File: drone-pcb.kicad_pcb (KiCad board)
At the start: 2 copper layers, 46 parts, among them J1 Conn_01x02_Pin, J10 Conn_01x03_Pin, J11 Conn_01x03_Pin, J12 Conn_01x03_Pin, J2 Conn_01x02_Pin, J3 Conn_01x02_Pin, J4 Conn_01x02_Pin, J5 Conn_01x02_Pin, J6 Conn_01x02_Pin, J7 USB_C_Receptacle_USB2.0_16P, J8 Conn_01x02_Pin, J9 Conn_01x03_Pin, Q1 AO3400A, Q2 AO3400A, Q3 AO3400A, Q4 AO3400A, Q5 AO3400A, Q6 AO3400A, SW1 CK_KMS2xxGP, U1 STM32F030C8Tx, U2 nRF24L01P, U3 MCP73831-2-OT, U4 TLV75533PDBV

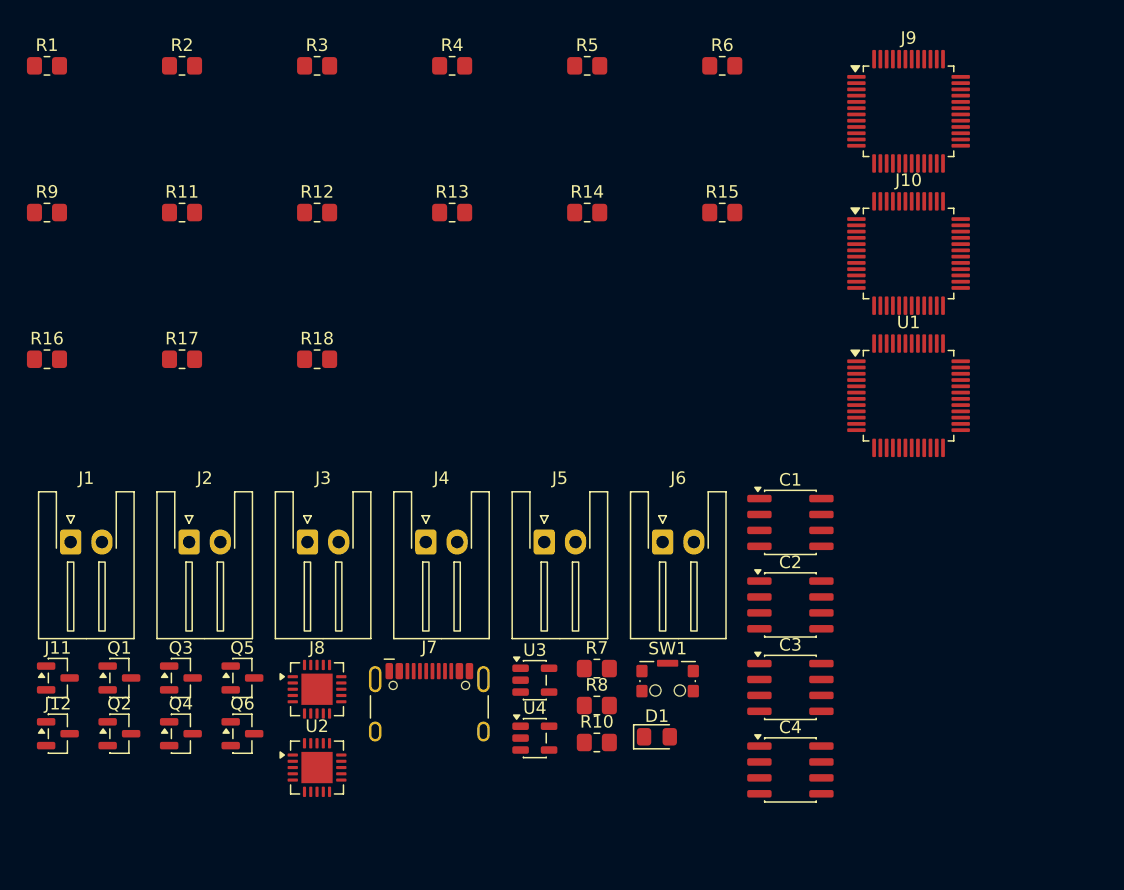
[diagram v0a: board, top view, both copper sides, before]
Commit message: svg images for board and schematic
inserted in README.md too
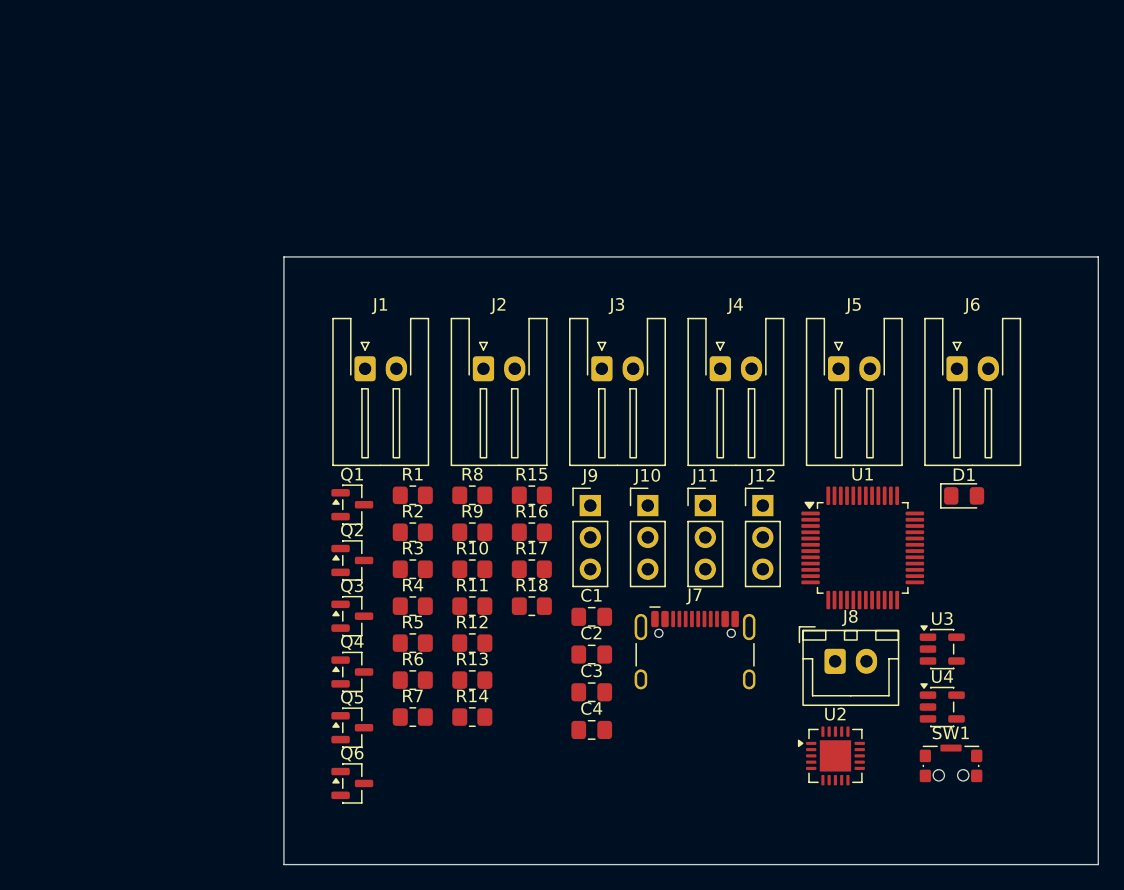
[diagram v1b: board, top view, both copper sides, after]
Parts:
- C1, C2, C3, C4: footprint Package_SO:SOIC-8_3.9x4.9mm_P1.27mm -> Capacitor_SMD:C_0805_2012Metric_Pad1.18x1.45mm_HandSolder
- J10, J9: footprint Package_QFP:LQFP-48_7x7mm_P0.5mm -> Connector_PinHeader_2.54mm:PinHeader_1x03_P2.54mm_Vertical
- J11, J12: footprint Package_TO_SOT_SMD:SOT-23 -> Connector_PinHeader_2.54mm:PinHeader_1x03_P2.54mm_Vertical
- J8: footprint Package_DFN_QFN:QFN-20-1EP_4x4mm_P0.5mm_EP2.5x2.5mm -> Connector_JST:JST_XH_B2B-XH-A_1x02_P2.50mm_Vertical
- moved J12 59.1 mm to (161.2, 96.8)
- moved R6 54.9 mm to (133.3, 110.8)
- moved J11 53.5 mm to (156.6, 96.8)
- moved R5 48.1 mm to (133.3, 107.8)
- moved R1 45.0 mm to (133.3, 96.0)
- moved R4 43.2 mm to (133.3, 104.9)
- moved R9 42.5 mm to (138.0, 99.0)
- moved R2 41.5 mm to (133.3, 99.0)
- moved J8 41.4 mm to (167.0, 109.3)
- moved U2 41.4 mm to (167.0, 116.8)
- moved R14 41.3 mm to (138.0, 113.7)
- moved R16 41.1 mm to (142.8, 99.0)
- moved R3 40.9 mm to (133.3, 101.9)
- moved J9 40.4 mm to (147.5, 96.8)
- moved R11 39.0 mm to (138.0, 104.9)
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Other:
- board outline added: 65 x 48.5 mm
